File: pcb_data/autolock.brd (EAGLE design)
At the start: 65 x 56 mm, 20 parts, among them CN1 RASPBERRYPI-GPIO, T1 2SC1815

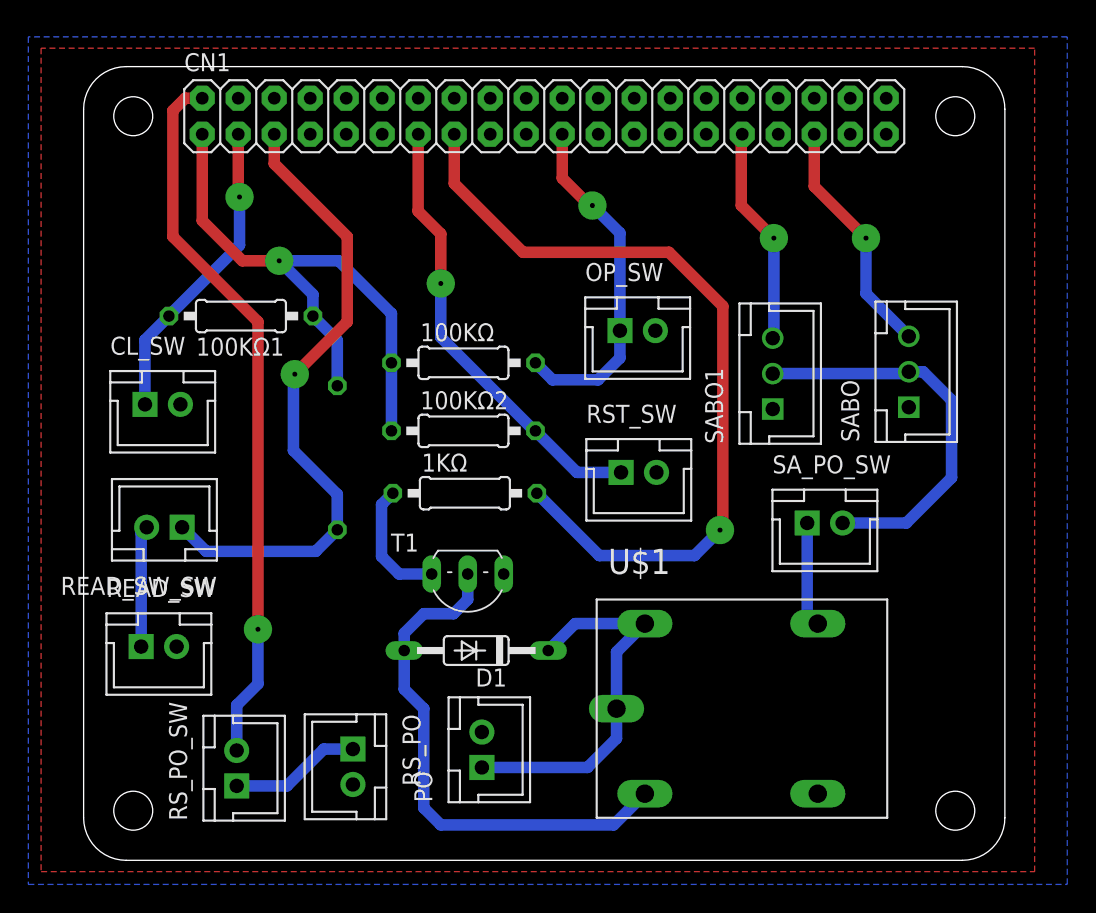
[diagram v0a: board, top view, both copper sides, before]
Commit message: 基板GND周り修正、実装図追加
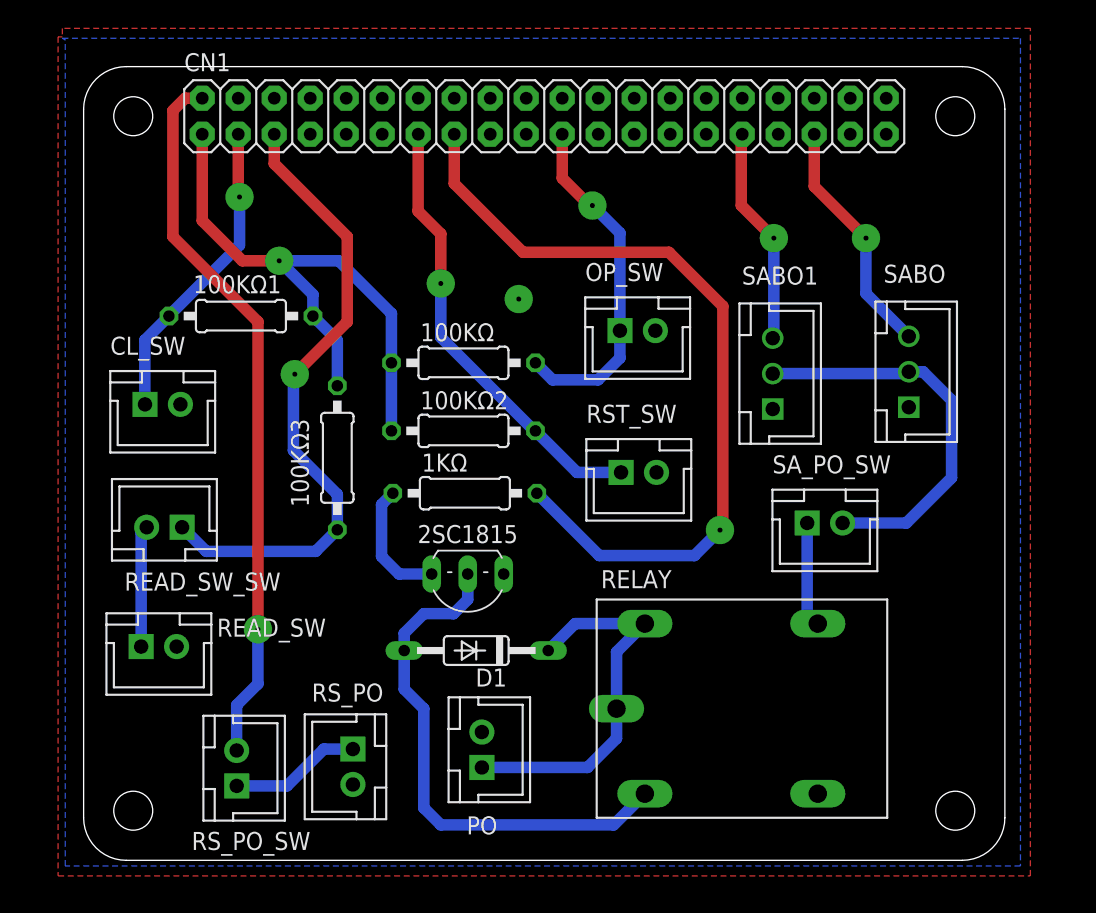
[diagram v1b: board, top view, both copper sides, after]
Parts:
- flipped 100KΩ3 to the top
- renumbered T1 to 2SC1815, U$1 to RELAY
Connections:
- net GND: now also CN1.14, CN1.20, CN1.25, CN1.30, CN1.34, CN1.6, CN1.9
